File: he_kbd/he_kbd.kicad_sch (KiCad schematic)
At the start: 54 parts, among them J1 AudioJack4, J2 Conn_01x08_Pin

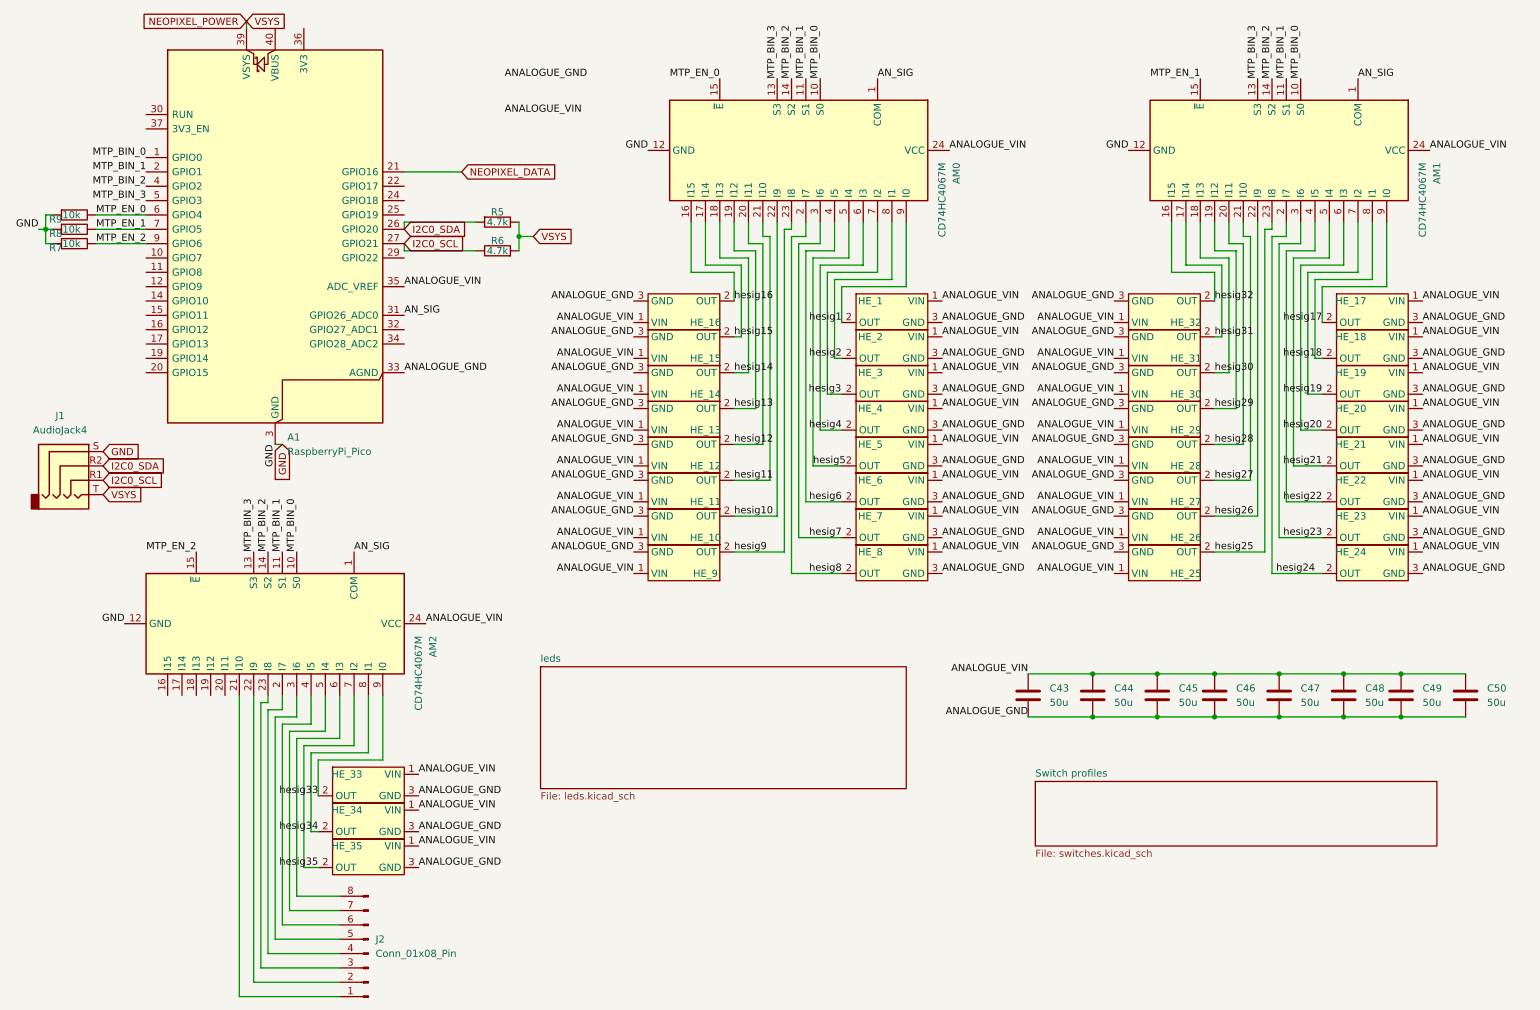
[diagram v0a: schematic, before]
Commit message: Updated footprints
Updated the footprints of the analogue sensor to join the sensor with
the keyswitch outline and holes

Changed to use the correct 3.3v output pin for power

Added 100nf capacitors to the multiplexers
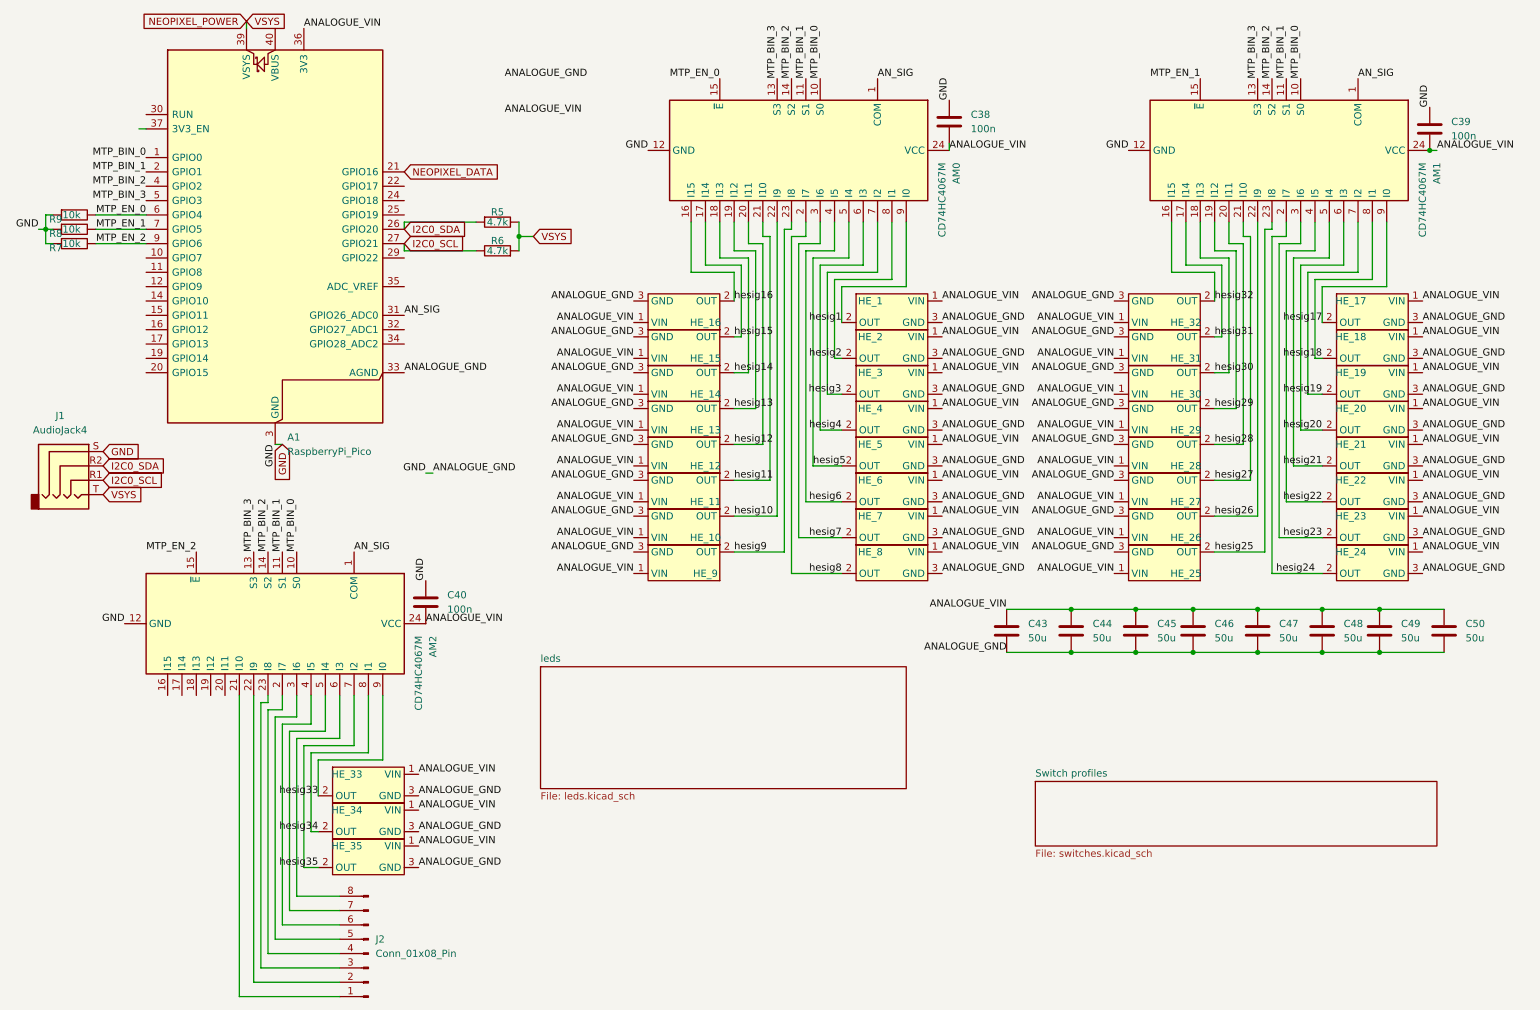
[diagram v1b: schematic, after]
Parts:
- added C38, C39, C40: 100n, PCM_Capacitor_SMD_AKL:C_0805_2012Metric_Pad1.18x1.45mm_HandSolder, symbol PCM_Capacitor_AKL:C_0805
- A1: footprint Module:RaspberryPi_Pico_Common_SMD -> Module:RaspberryPi_Pico_Common_Unspecified
- AM0, AM1, AM2: footprint Package_SO:SSOP-24_5.3x8.2mm_P0.65mm -> Package_SO:SOIC-24W_7.5x15.4mm_P1.27mm
- HE_1, HE_10, HE_11, HE_12, HE_13, HE_14, HE_15, HE_16, HE_17, HE_18, HE_19, HE_2, HE_20, HE_21, HE_22, HE_23, HE_24, HE_25, HE_26, HE_27, HE_28, HE_29, HE_3, HE_30, HE_31, HE_32, HE_33, HE_34, HE_35, HE_4, HE_5, HE_6, HE_7, HE_8, HE_9: footprint Package_TO_SOT_SMD:SOT-23-3 -> he_kbd_footprint:Analogue_sensor_and_switch_profile
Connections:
- net ANALOGUE_GND is gone; now on net GND: A1.33 (AGND), C43.2, C44.2, C45.2, C46.2, C47.2, C48.2, C49.2, C50.2, HE_1.3 (GND), HE_10.3 (GND), HE_11.3 (GND), HE_12.3 (GND), HE_13.3 (GND), HE_14.3 (GND), HE_15.3 (GND), HE_16.3 (GND), HE_17.3 (GND), HE_18.3 (GND), HE_19.3 (GND), HE_2.3 (GND), HE_20.3 (GND), HE_21.3 (GND), HE_22.3 (GND), HE_23.3 (GND), HE_24.3 (GND), HE_25.3 (GND), HE_26.3 (GND), HE_27.3 (GND), HE_28.3 (GND), HE_29.3 (GND), HE_3.3 (GND), HE_30.3 (GND), HE_31.3 (GND), HE_32.3 (GND), HE_33.3 (GND), HE_34.3 (GND), HE_35.3 (GND), HE_4.3 (GND), HE_5.3 (GND), HE_6.3 (GND), HE_7.3 (GND), HE_8.3 (GND), HE_9.3 (GND)
- net ANALOGUE_VIN: now also A1.36 (3V3), C38.1, C39.1, C40.1; no longer A1.35 (ADC_VREF)
- net GND: now also C38.2, C39.2, C40.2
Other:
- moved on the sheet: C43, C44, C45, C46, C47, C48, C49, C50
